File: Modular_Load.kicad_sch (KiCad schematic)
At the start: 52 parts, among them J1 Conn_02x04_Odd_Even, J2 Conn_Coaxial, J3 7466203, J4 Conn_Coaxial, J5 7466203, J6 Conn_Coaxial, J7 Conn_Coaxial, Q2 IGT65R025D2, U1 ADA4807-4

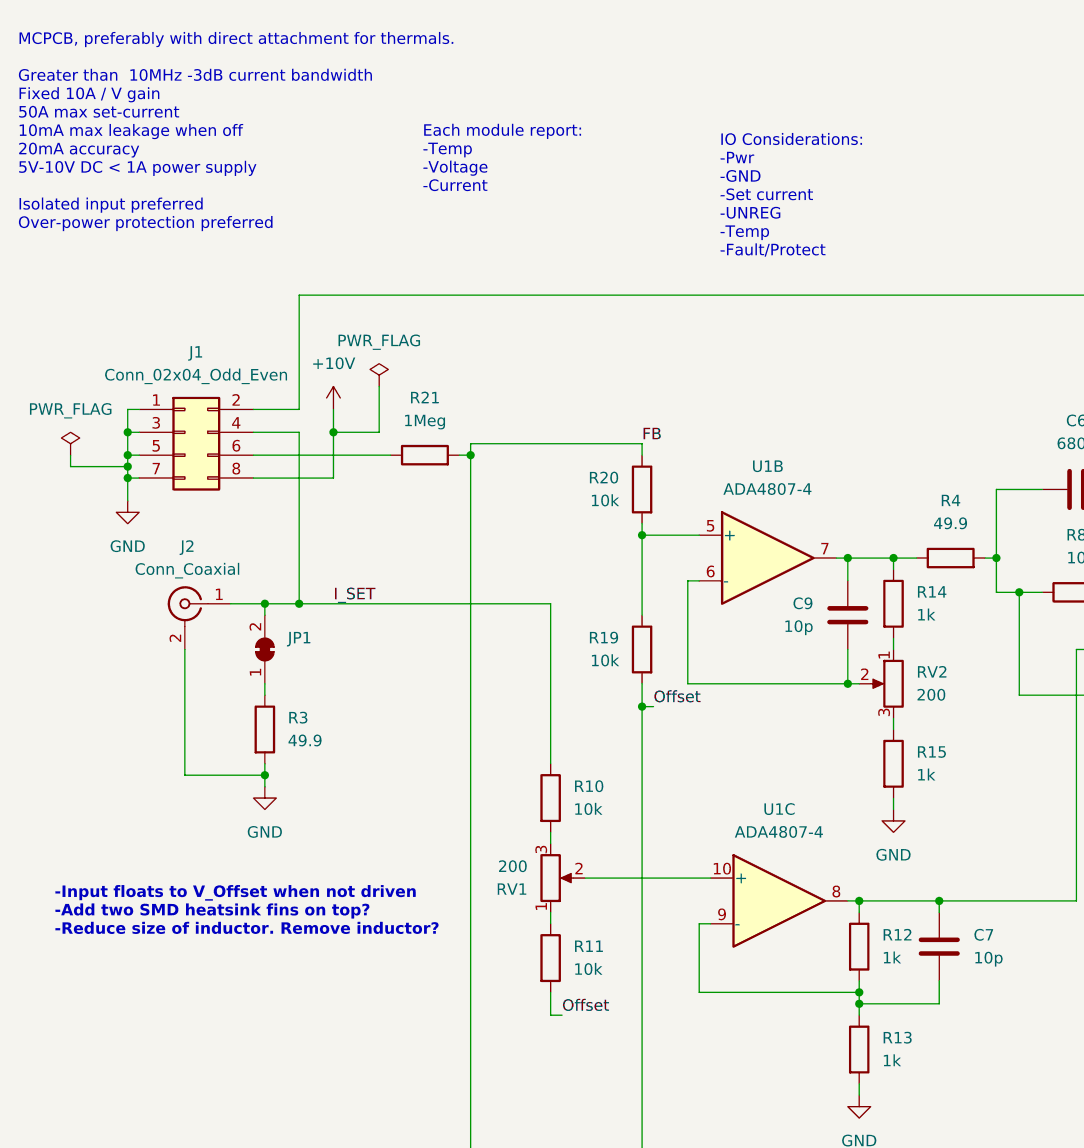
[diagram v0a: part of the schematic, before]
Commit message: Added heatsink drawings, updated component 3D models
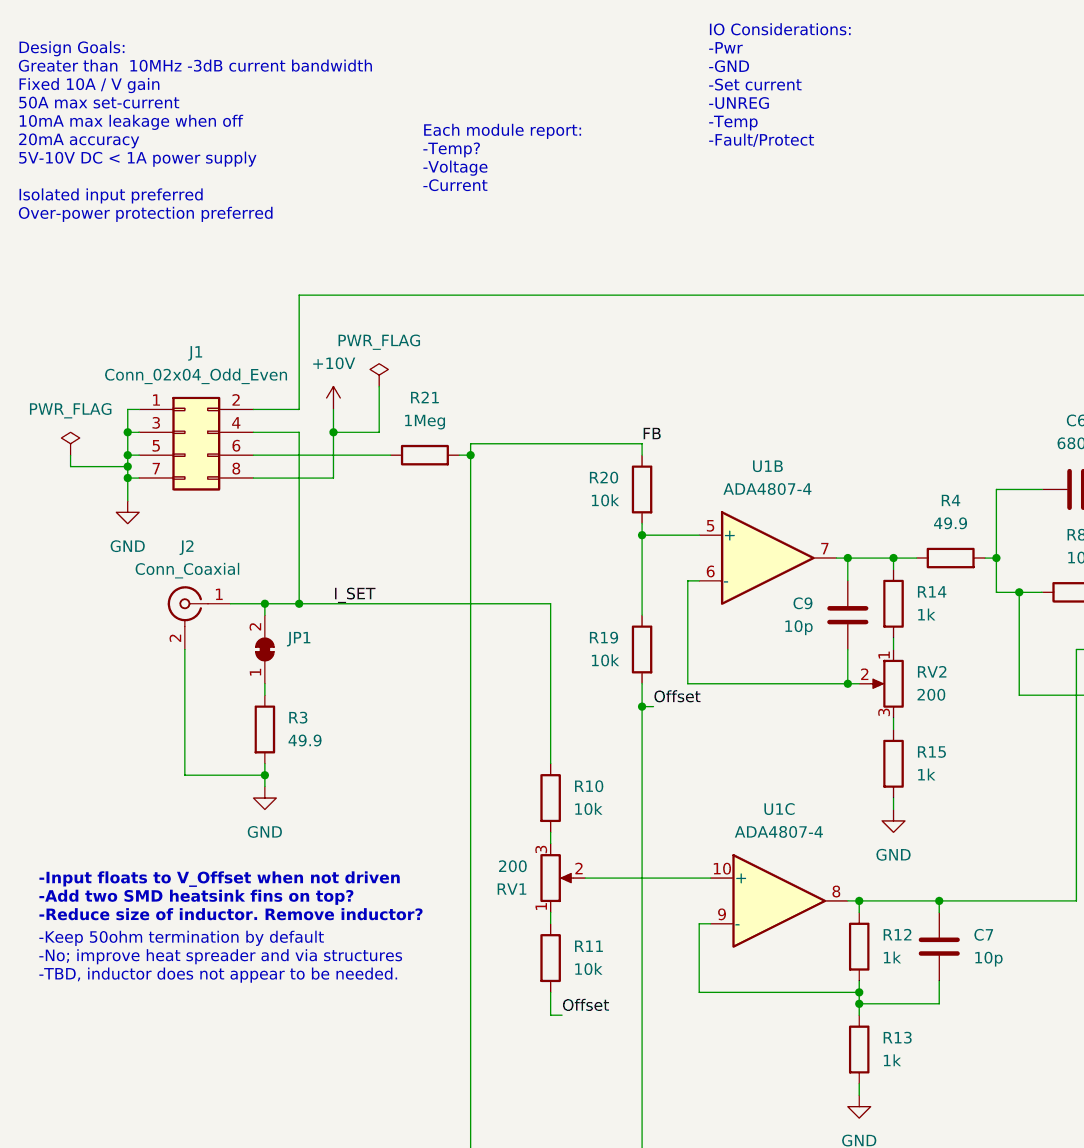
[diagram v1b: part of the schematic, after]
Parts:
- J1: Mates With (none) -> 71600-308LF
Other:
- note added: "-Keep 50ohm termination by default -No; improve heat spreader and via structures -TBD, inductor does not appear to be needed."
- note added: "Design Goals: Greater than 10MHz -3dB current bandwidth Fixed 10A / V gain 50A max set-current 10mA max leakage when off 20mA accuracy 5V-10V DC < 1A power supply Isolated input preferred Over-power protection preferred"
- note added: "Each module report: -Temp? -Voltage -Current"
- note removed: "Each module report: -Temp -Voltage -Current"
- note removed: "MCPCB, preferably with direct attachment for thermals. Greater than 10MHz -3dB current bandwidth Fixed 10A / V gain 50A max set-current 10mA max leakage when off 20mA accuracy 5V-10V DC < 1A power supply Isolated input preferred Over-power protection preferred"
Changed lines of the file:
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@@
 	(text "IO Considerations:\n-Pwr\n-GND\n-Set current\n-UNREG\n-Temp\n-Fault/Protect"
 		(exclude_from_sim no)
-		(at 92.456 26.67 0)
+		(at 91.186 14.478 0)
 		(effects
 			(font
@@
 	(text "-Input floats to V_Offset when not driven\n-Add two SMD heatsink fins on top?\n-Reduce size of inductor. Remove inductor?"
 		(exclude_from_sim no)
-		(at 18.542 110.236 0)
+		(at 16.764 108.712 0)
 		(effects
 			(font
@@
 		)
 	)
-	(text "MCPCB, preferably with direct attachment for thermals.\n\nGreater than  10MHz -3dB current bandwidth\nFixed 10A / V gain\n50A max set-current\n10mA max leakage when off\n20mA accuracy\n5V-10V DC < 1A power supply\n\nIsolated input preferred\nOver-power protection preferred\n"
+	(text "Design Goals:\nGreater than  10MHz -3dB current bandwidth\nFixed 10A / V gain\n50A max set-current\n10mA max leakage when off\n20mA accuracy\n5V-10V DC < 1A power supply\n\nIsolated input preferred\nOver-power protection preferred\n"
 		(exclude_from_sim no)
 		(at 14.478 26.416 0)
@@
 		)
 	)
-	(text "Each module report:\n-Temp\n-Voltage\n-Current"
+	(text "-Keep 50ohm termination by default\n-No; improve heat spreader and via structures\n-TBD, inductor does not appear to be needed."
+		(exclude_from_sim no)
+		(at 16.764 115.316 0)
+		(effects
+			(font
+				(size 1.27 1.27)
+			)
+			(justify left top)
+		)
+	)
+	(text "Each module report:\n-Temp?\n-Voltage\n-Current"
 		(exclude_from_sim no)
 		(at 59.436 29.464 0)
@@
 			)
 		)
+		(property "Mates With" "71600-308LF"
+			(at 33.02 59.69 0)
+			(effects
+				(font
+					(size 1.27 1.27)
+				)
+				(hide yes)
+			)
+		)
 		(pin "6"
 		)
@@
 			(effects
 				(font
-					(size 1.27 1.27)
-				)
-				(hide yes)
-			)
-		)
-		(property "Mates with" ""
-			(at 193.04 83.82 0)
-			(effects
-				(font
